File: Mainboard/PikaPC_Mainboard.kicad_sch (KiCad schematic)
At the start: 87 parts, among them J1 Conn_02x08_Odd_Even, J10 Conn_01x08, J11 Conn_01x08, J12 Conn_01x08, J13 Conn_01x08, J14 Conn_01x08, J15 Conn_01x08, J16 Conn_01x08, J17 Conn_01x08, J18 Conn_01x10, J19 Conn_02x05_Odd_Even, J5 DIN41612_03x32_C_Split, J6 Mini-DIN-6, J7 Mini-DIN-6, J9 Conn_01x08, SW1 SW_Push_DPDT, SW2 SW_Push, U1 PPC403GA, U10 74LS07, U11 86C325, U12 GD75232N, U13 74LVC125, U14 MCP120-315GI/TO, U15 AS6C4008-55PCN, U16 AS6C4008-55PCN, U17 ATF1504, U18 T224162B, U19 T224162B, U2 SN74LVC245A, U20 T224162B, U21 T224162B, U22 SN74LVC245A, U23 SN74LVC245A, U3 SST39VF010, U4 SN74LVC245A, U5 SN74LVC245A, U6 SN74LVC245A, U7 8042 PS/2, U8 SN74LVC245A, U9 74LS04, Y1 25M, Y2 7M3728, Y3 14M31818

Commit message: VRAM control debugging
- correct clock edge for VLB ReadyIn
- minor tweaks for S3 ViRGE symbol
- add series resistors to VRAM control signals
- add strapping resistor to support Trio64V+
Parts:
- added RN10, RN11, RN12: 33R, Resistor_THT:R_Array_SIP10, symbol Device:R_Pack05_SIP_Split
- added RN9: 10X-1-472LF, Resistor_THT:R_Array_SIP10, symbol Device:R_Network09_US
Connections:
- net +5V: now also RN9.1 (common)
- net VID-SAUP2: now also RN5.2 (R1)
- net VMA0: now also RN11.1 (R1.1)
- net VMA1: now also RN11.3 (R2.1)
- net VMA2: now also RN11.5 (R3.1)
- net VMA3: now also RN11.7 (R4.1)
- net VMA4: now also RN11.9 (R5.1)
- net VMA5: now also RN12.1 (R1.1)
- net VMA6: now also RN12.3 (R2.1)
- net VMA7: now also RN12.5 (R3.1)
- net VMA8: now also RN12.7 (R4.1)
- net VMD24: now also RN6.7 (R6)
- net ~{VMOE}: now also RN10.5 (R3.1); no longer U18.27 (~{OE}), U19.27 (~{OE}), U20.27 (~{OE}), U21.27 (~{OE})
- net ~{VMRAS0}: now also RN10.1 (R1.1); no longer U18.14 (~{RAS}), U19.14 (~{RAS}), U20.14 (~{RAS}), U21.14 (~{RAS})
- net ~{VMWE}: now also RN10.3 (R2.1); no longer U18.13 (~{WE}), U19.13 (~{WE}), U20.13 (~{WE}), U21.13 (~{WE})
- net VLCLK: now reaches U11.148 (LCLK)
- net VLCLK: now also RN9.2 (R1)
- net VEVIDEO: now reaches U11.203 (~{VREQ})
- net VEVIDEO: now also RN9.5 (R4)
- net ~{VCREQ}: now reaches U11.204 (~{CREQ})
- net ~{VCREQ}: now also RN9.3 (R2)
- net VESYNC: now reaches U11.205 (SPCLK)
- net VESYNC: now also RN9.4 (R3)
- net ~{VBLANK}: now reaches U11.206 (SPD)
- net ~{VBLANK}: now also RN9.6 (R5)
- new net ~{VMOER}: RN10.6 (R3.2), U18.27 (~{OE}), U19.27 (~{OE}), U20.27 (~{OE}), U21.27 (~{OE})
- new net ~{VMRAS0R}: RN10.2 (R1.2), U18.14 (~{RAS}), U19.14 (~{RAS}), U20.14 (~{RAS}), U21.14 (~{RAS})
- new net ~{VMWER}: RN10.4 (R2.2), U18.13 (~{WE}), U19.13 (~{WE}), U20.13 (~{WE}), U21.13 (~{WE})
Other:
- note added: "VMD24 for LPB Mode on Trio64V+"
- moved on the sheet: FB1, FB2, FB3, J1, R11, R6, R7, RN1, RN2, RN3, RN5, U11A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

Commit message: Add new bus to wire-wrap mainboard
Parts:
- removed C19, C20, C21, C22: 47p, Capacitor_THT:C_Disc_D3.0mm_W2.0mm_P2.50mm, symbol Device:C_Small_US
- removed C23, C24: 100nF, Capacitor_THT:C_Disc_D3.0mm_W2.0mm_P2.50mm, symbol Device:C_Small_US
- removed FB1, FB2, FB3: FerriteBead, Inductor_THT:L_Axial_L7.0mm_D3.3mm_P5.08mm_Vertical_Fastron_MICC, symbol Device:FerriteBead
- removed J1: Conn_02x08_Odd_Even, Connector_PinHeader_2.54mm:PinHeader_2x08_P2.54mm_Vertical, symbol Connector_Generic:Conn_02x08_Odd_Even
- removed J6, J7: Mini-DIN-6, Connector_PinHeader_2.54mm:PinHeader_2x03_P2.54mm_Vertical, symbol Connector:Mini-DIN-6
- removed R11, R6, R7: 75R, Resistor_THT:R_Axial_DIN0204_L3.6mm_D1.6mm_P2.54mm_Vertical, symbol Device:R_Small_US
- removed R2: 220R, Resistor_THT:R_Axial_DIN0204_L3.6mm_D1.6mm_P2.54mm_Vertical, symbol Device:R_Small_US
- removed R3: 470R, Resistor_THT:R_Axial_DIN0204_L3.6mm_D1.6mm_P2.54mm_Vertical, symbol Device:R_Small_US
- removed RN10, RN11, RN12: 33R, Resistor_THT:R_Array_SIP10, symbol Device:R_Pack05_SIP_Split
- removed RN4, RN6, RN8: 9A103J, Resistor_THT:R_Array_SIP9, symbol Device:R_Network08_US
- removed RN7: 10X-1-472F, Resistor_THT:R_Array_SIP9, symbol Device:R_Network08_US
- removed RN9: 10X-1-472LF, Resistor_THT:R_Array_SIP10, symbol Device:R_Network09_US
- removed unit 4 of U10
- removed unit 1 of U10
- removed unit 2 of U10
- removed unit 3 of U10
- removed U11: 86C325, Package_QFP:PQFP-208_28x28mm_P0.5mm, symbol PikaPC:S3 86C325 ViRGE
- removed U17: ATF1504, Package_LCC:PLCC-44_THT-Socket, symbol Wrap030-ATX:ATF1504AS
- removed U18, U19, U20, U21: T224162B, Package_SO:SOJ-44_10.16x28.575mm_P1.27mm, symbol PikaPC:T224162B-xJ
- removed U7: 8042 PS/2, Package_DIP:DIP-40_W15.24mm_Socket, symbol MCU_Intel:8040
- removed unit 2 of U9
- removed unit 3 of U9
- removed unit 4 of U9
- removed unit 1 of U9
- removed Y3: 14M31818, Oscillator:Oscillator_DIP-8, symbol Oscillator:CXO_DIP8
- added U102: SN74LVC245A, Package_DIP:DIP-20_W7.62mm_Socket, symbol 74xx:74LS245
- added U109, U110, U111, U112: 74LS244, Package_DIP:DIP-20_W7.62mm_Socket, symbol 74xx:74LS244
- added U2: ATF1508AS, Package_LCC:PLCC-84_THT-Socket, symbol PikaPC:ATF1508AS
- renumbered U8 to U101, U22 to U103, U23 to U104, U2 to U105, U4 to U106, U5 to U107, U6 to U108
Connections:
- net VD0 is gone; now on net D31: U106.2 (A0)
- net VD1 is gone; now on net D30: U106.3 (A1)
- net VD10 is gone; now on net D29: U101.4 (A2), U105.4 (A2)
- net VD11 is gone; now on net D28: U101.5 (A3), U105.5 (A3)
- net VD12 is gone; now on net D27: U101.6 (A4), U105.6 (A4)
- net VD13 is gone; now on net D26: U101.7 (A5), U105.7 (A5)
- net VD14 is gone; now on net D25: U101.8 (A6), U105.8 (A6)
- net VD15 is gone; now on net D24: U101.9 (A7), U105.9 (A7)
- net VD2 is gone; now on net D29: U106.4 (A2)
- net VD3 is gone; now on net D28: U106.5 (A3)
- net VD4 is gone; now on net D27: U106.6 (A4)
- net VD5 is gone; now on net D26: U106.7 (A5)
- net VD6 is gone; now on net D25: U106.8 (A6)
- net VD7 is gone; now on net D24: U106.9 (A7)
- net VD8 is gone; now on net D31: U101.2 (A0), U105.2 (A0)
- net VD9 is gone; now on net D30: U101.3 (A1), U105.3 (A1)
- net ~{PBE2} is gone; now on net ~{BEN-32}: U103.19 (CE)
- net ~{PBE3} is gone; now on net ~{BEN-32}: U104.19 (CE)
- net +12V: now also J5.a30 (Pin_a30)
- net +3.3V: now also J5.a22 (Pin_a22), J5.a23 (Pin_a23), J5.b5 (Pin_b5), J5.b6 (Pin_b6), U102.20 (VCC)
- net +5V: now also J5.a2 (Pin_a2), J5.a31 (Pin_a31), J5.b2 (Pin_b2), J5.b3 (Pin_b3), J5.b31 (Pin_b31), J5.b4 (Pin_b4), J5.c2 (Pin_c2), J5.c31 (Pin_c31), U109.20 (VCC), U110.20 (VCC), U111.20 (VCC), U112.20 (VCC), U2.13 (VCCIO), U2.26 (VCCIO), U2.3 (VCC), U2.38 (VCCIO), U2.43 (VCC), U2.53 (VCCIO), U2.66 (VCCIO), U2.78 (VCCIO)
- net -12V: now also J5.c30 (Pin_c30)
- net A0/~{WBE0}: now also U2.41 (IO49)
- net A10: now also U110.6 (I2a)
- net A11: now also U110.8 (I3a)
- net A12: now also U110.11 (I0b)
- net A13: now also U110.13 (I1b)
- net A14: now also U110.15 (I2b)
- net A15: now also U110.17 (I3b)
- net A16: now also U111.2 (I0a)
- net A17: now also U111.4 (I1a)
- net A18: now also U111.6 (I2a)
- net A19: now also U111.8 (I3a)
- net A1/~{WBE1}: now also U2.40 (IO51)
- net A2: now also U109.6 (I2a)
- net A20: now also U111.11 (I0b)
- net A21: now also U111.13 (I1b)
- net A22: now also U111.15 (I2b)
- net A23: now also U111.17 (I3b)
- net A24: now also U112.2 (I0a)
- net A25: now also U112.4 (I1a)
- net A3: now also U109.8 (I3a)
- net A4: now also U109.11 (I0b)
- net A5: now also U109.13 (I1b)
- net A6: now also U109.15 (I2b)
- net A7: now also U109.17 (I3b)
- net A8: now also U110.2 (I0a)
- net A9: now also U110.4 (I1a)
- net D0: now also U104.9 (A7); no longer U107.18 (B0)
- net D1: now also U104.8 (A6); no longer U107.17 (B1)
- net D10: now also U103.7 (A5); no longer U108.16 (B2)
- net D11: now also U103.6 (A4); no longer U108.15 (B3)
- net D12: now also U103.5 (A3); no longer U108.14 (B4)
- net D13: now also U103.4 (A2); no longer U108.13 (B5)
- net D14: now also U103.3 (A1); no longer U108.12 (B6)
- net D15: now also U103.2 (A0); no longer U108.11 (B7)
- net D16: now also U108.9 (A7), U102.9 (A7); no longer U105.18 (B0)
- net D17: now also U108.8 (A6), U102.8 (A6); no longer U105.17 (B1)
- net D18: now also U108.7 (A5), U102.7 (A5); no longer U105.16 (B2)
- net D19: now also U108.6 (A4), U102.6 (A4); no longer U105.15 (B3)
- net D2: now also U104.7 (A5); no longer U107.16 (B2)
- net D20: now also U108.5 (A3), U102.5 (A3); no longer U105.14 (B4)
- net D21: now also U108.4 (A2), U102.4 (A2); no longer U105.13 (B5)
- net D22: now also U108.3 (A1), U102.3 (A1); no longer U105.12 (B6)
- net D23: now also U108.2 (A0), U102.2 (A0); no longer U105.11 (B7)
- net D24: now also U107.9 (A7); no longer U101.18 (B0), U103.18 (B0), U104.18 (B0), U106.18 (B0)
- net D25: now also U107.8 (A6); no longer U101.17 (B1), U103.17 (B1), U104.17 (B1), U106.17 (B1)
- net D26: now also U107.7 (A5); no longer U101.16 (B2), U103.16 (B2), U104.16 (B2), U106.16 (B2)
- net D27: now also U107.6 (A4); no longer U101.15 (B3), U103.15 (B3), U104.15 (B3), U106.15 (B3)
- net D28: now also U107.5 (A3); no longer U101.14 (B4), U103.14 (B4), U104.14 (B4), U106.14 (B4)
- net D29: now also U107.4 (A2); no longer U101.13 (B5), U103.13 (B5), U104.13 (B5), U106.13 (B5)
- net D3: now also U104.6 (A4); no longer U107.15 (B3)
- net D30: now also U107.3 (A1); no longer U101.12 (B6), U103.12 (B6), U104.12 (B6), U106.12 (B6)
- net D31: now also U107.2 (A0); no longer U101.11 (B7), U103.11 (B7), U104.11 (B7), U106.11 (B7)
- net D4: now also U104.5 (A3); no longer U107.14 (B4)
- net D5: now also U104.4 (A2); no longer U107.13 (B5)
- net D6: now also U104.3 (A1); no longer U107.12 (B6)
- net D7: now also U104.2 (A0); no longer U107.11 (B7)
- net D8: now also U103.9 (A7); no longer U108.18 (B0)
- net D9: now also U103.8 (A6); no longer U108.17 (B1)
- net GND: now also J5.a1 (Pin_a1), J5.a28 (Pin_a28), J5.a32 (Pin_a32), J5.b1 (Pin_b1), J5.b10 (Pin_b10), J5.b11 (Pin_b11), J5.b12 (Pin_b12), J5.b13 (Pin_b13), J5.b14 (Pin_b14), J5.b15 (Pin_b15), J5.b16 (Pin_b16), J5.b17 (Pin_b17), J5.b18 (Pin_b18), J5.b19 (Pin_b19), J5.b20 (Pin_b20), J5.b21 (Pin_b21), J5.b28 (Pin_b28), J5.b29 (Pin_b29), J5.b30 (Pin_b30), J5.b32 (Pin_b32), J5.b7 (Pin_b7), J5.b8 (Pin_b8), J5.b9 (Pin_b9), J5.c1 (Pin_c1), J5.c29 (Pin_c29), J5.c32 (Pin_c32), U102.10 (GND), U109.10 (GND), U109.2 (I0a), U109.4 (I1a), U110.10 (GND), U111.10 (GND), U112.10 (GND), U112.17 (I3b), U112.6 (I2a), U112.8 (I3a), U2.19 (GND), U2.32 (GND), U2.42 (GND), U2.47 (GND), U2.59 (GND), U2.7 (GND), U2.72 (GND), U2.82 (GND)
- net HoldAck: now also U2.49 (IO73)
- net HoldReq: now also U2.48 (IO72)
- net INT0: now also U2.67 (IO104)
- net INT1: now also U2.68 (IO105)
- net INT2: now also U2.69 (IO107)
- net INT3: now also U2.70 (IO109)
- net INT4: now also U2.73 (IO115)
- net Ready: now also U2.50 (IO75)
- net R/~{W}: now also U2.12 (IO3); no longer U101.1 (A->B), U103.1 (A->B), U104.1 (A->B), U105.1 (A->B), U106.1 (A->B), U107.1 (A->B), U108.1 (A->B)
- net SysClk-5v: now also U2.83 (GCLK1)
- net ~{CINT}: now also U2.44 (IO65)
- net ~{CS0}: now also U2.54 (IO83)
- net ~{CS1}: now also U2.55 (IO85)
- net ~{CS2}: now also U2.56 (IO86)
- net ~{CS3}: now also U2.57 (IO88)
- net ~{CS4}: now also U2.58 (IO91)
- net ~{CS5}: now also U2.60 (IO93)
- net ~{CS6}: now also U2.61 (IO94)
- net ~{CS7}: now also U2.63 (IO97)
- net ~{Reset}: now also U2.1 (GCLR)
- net ~{WBE2}: now also U2.39 (IO53)
- net ~{WBE3}: now also U2.37 (IO56)
- net AD8: now reaches J5.c10 (Pin_c10)
- net AD8: now also U103.11 (B7), U106.11 (B7), U110.18 (O0a)
- net AD10: now reaches J5.c11 (Pin_c11)
- net AD10: now also U103.13 (B5), U106.13 (B5), U110.14 (O2a)
- net AD12: now reaches J5.c12 (Pin_c12)
- net AD12: now also U103.15 (B3), U106.15 (B3), U110.9 (O0b)
- net AD14: now reaches J5.c13 (Pin_c13)
- net AD14: now also U103.17 (B1), U106.17 (B1), U110.5 (O2b)
- net AD16: now reaches J5.c14 (Pin_c14)
- net AD16: now also U105.11 (B7), U102.11 (B7), U111.18 (O0a)
- net AD18: now reaches J5.c15 (Pin_c15)
- net AD18: now also U105.13 (B5), U102.13 (B5), U111.14 (O2a)
- net AD20: now reaches J5.c16 (Pin_c16)
- net AD20: now also U105.15 (B3), U102.15 (B3), U111.9 (O0b)
- net AD22: now reaches J5.c17 (Pin_c17)
- net AD22: now also U105.17 (B1), U102.17 (B1), U111.5 (O2b)
- net AD24: now reaches J5.c18 (Pin_c18)
- net AD24: now also U101.11 (B7), U112.18 (O0a)
- net AD26: now reaches J5.c19 (Pin_c19)
- net AD26: now also U101.13 (B5), U112.14 (O2a)
- net AD28: now reaches J5.c20 (Pin_c20)
- net AD28: now also U101.15 (B3), U112.9 (O0b)
- net AD30: now reaches J5.c21 (Pin_c21)
- net AD30: now also U101.17 (B1), U112.5 (O2b)
- net ~{Bus-REQ}: now reaches J5.c22 (Pin_c22)
- net ~{Bus-REQ}: now also U2.77 (IO123)
- net ~{Bus-GNT}: now reaches J5.c23 (Pin_c23)
- net ~{Bus-GNT}: now also U2.81 (IO128)
- net ~{Bus-BE0}: now reaches J5.c24 (Pin_c24)
- net ~{Bus-BE0}: now also U2.21 (IO19)
- net ~{Bus-BE2}: now reaches J5.c25 (Pin_c25)
- net ~{Bus-BE2}: now also U2.16 (IO27)
- net ~{Bus-BRACK}: now reaches J5.c26 (Pin_c26)
- net ~{Bus-Start}: now reaches J5.c27 (Pin_c27)
- net ~{Bus-Start}: now also U2.15 (IO29)
- net ~{Bus-BERR}: now reaches J5.c28 (Pin_c28)
- net ~{Bus-Reset}: now reaches J5.c3 (Pin_c3)
- net ~{Bus-IACK}: now reaches J5.c4 (Pin_c4)
- net Bus-R/~{W}: now reaches J5.c5 (Pin_c5)
- net AD0: now reaches J5.c6 (Pin_c6)
- net AD0: now also U104.11 (B7), U107.11 (B7), U108.11 (B7), U109.18 (O0a)
- net AD2: now reaches J5.c7 (Pin_c7)
- net AD2: now also U104.13 (B5), U107.13 (B5), U108.13 (B5), U109.14 (O2a)
- net AD4: now reaches J5.c8 (Pin_c8)
- net AD4: now also U104.15 (B3), U107.15 (B3), U108.15 (B3), U109.9 (O0b)
- net AD6: now reaches J5.c9 (Pin_c9)
- net AD6: now also U104.17 (B1), U107.17 (B1), U108.17 (B1), U109.5 (O2b)
- net AD9: now reaches J5.a10 (Pin_a10)
- net AD9: now also U103.12 (B6), U106.12 (B6), U110.16 (O1a)
- net AD11: now reaches J5.a11 (Pin_a11)
- net AD11: now also U103.14 (B4), U106.14 (B4), U110.12 (O3a)
- net AD13: now reaches J5.a12 (Pin_a12)
- net AD13: now also U103.16 (B2), U106.16 (B2), U110.7 (O1b)
- net AD15: now reaches J5.a13 (Pin_a13)
- net AD15: now also U103.18 (B0), U106.18 (B0), U110.3 (O3b)
- net AD17: now reaches J5.a14 (Pin_a14)
- net AD17: now also U105.12 (B6), U102.12 (B6), U111.16 (O1a)
- net AD19: now reaches J5.a15 (Pin_a15)
- net AD19: now also U105.14 (B4), U102.14 (B4), U111.12 (O3a)
- net AD21: now reaches J5.a16 (Pin_a16)
- net AD21: now also U105.16 (B2), U102.16 (B2), U111.7 (O1b)
- net AD23: now reaches J5.a17 (Pin_a17)
- net AD23: now also U105.18 (B0), U102.18 (B0), U111.3 (O3b)
- net AD25: now reaches J5.a18 (Pin_a18)
- net AD25: now also U101.12 (B6), U112.16 (O1a)
- net AD27: now reaches J5.a19 (Pin_a19)
- net AD27: now also U101.14 (B4), U112.12 (O3a)
- net AD29: now reaches J5.a20 (Pin_a20)
- net AD29: now also U101.16 (B2), U112.7 (O1b)
- net AD31: now reaches J5.a21 (Pin_a21)
- net AD31: now also U101.18 (B0), U112.3 (O3b)
- net ~{Bus-BE1}: now reaches J5.a24 (Pin_a24)
- net ~{Bus-BE1}: now also U2.18 (IO24)
- net ~{Bus-BE3}: now reaches J5.a25 (Pin_a25)
- net ~{Bus-BE3}: now also U2.17 (IO25)
- net ~{Bus-BURST}: now reaches J5.a26 (Pin_a26)
- net ~{Bus-ACK}: now reaches J5.a27 (Pin_a27)
- net ~{Bus-ACK}: now also U2.20 (IO21)
- net Bus-Clk: now reaches J5.a29 (Pin_a29)
- net ~{Bus-IRQ0}: now reaches J5.a3 (Pin_a3)
- net ~{Bus-IRQ0}: now also U2.6 (IO13)
- net ~{Bus-IRQ1}: now reaches J5.a4 (Pin_a4)
- net ~{Bus-IRQ1}: now also U2.5 (IO14)
- net ~{Bus-IRQ2}: now reaches J5.a5 (Pin_a5)
- net ~{Bus-IRQ2}: now also U2.4 (IO16)
- net AD1: now reaches J5.a6 (Pin_a6)
- net AD1: now also U104.12 (B6), U107.12 (B6), U108.12 (B6), U109.16 (O1a)
- net AD3: now reaches J5.a7 (Pin_a7)
- net AD3: now also U104.14 (B4), U107.14 (B4), U108.14 (B4), U109.12 (O3a)
- net AD5: now reaches J5.a8 (Pin_a8)
- net AD5: now also U104.16 (B2), U107.16 (B2), U108.16 (B2), U109.7 (O1b)
- net AD7: now reaches J5.a9 (Pin_a9)
- net AD7: now also U104.18 (B0), U107.18 (B0), U108.18 (B0), U109.3 (O3b)
- removed net VD16: U103.2 (A0), U108.2 (A0)
- removed net VD17: U103.3 (A1), U108.3 (A1)
- removed net VD18: U103.4 (A2), U108.4 (A2)
- removed net VD19: U103.5 (A3), U108.5 (A3)
- removed net VD20: U103.6 (A4), U108.6 (A4)
- removed net VD21: U103.7 (A5), U108.7 (A5)
- removed net VD22: U103.8 (A6), U108.8 (A6)
- removed net VD23: U103.9 (A7), U108.9 (A7)
- removed net VD24: U104.2 (A0), U107.2 (A0)
- removed net VD25: U104.3 (A1), U107.3 (A1)
- removed net VD26: U104.4 (A2), U107.4 (A2)
- removed net VD27: U104.5 (A3), U107.5 (A3)
- removed net VD28: U104.6 (A4), U107.6 (A4)
- removed net VD29: U104.7 (A5), U107.7 (A5)
- removed net VD30: U104.8 (A6), U107.8 (A6)
- removed net VD31: U104.9 (A7), U107.9 (A7)
- removed net ~{PB32}: U105.19 (CE), U107.19 (CE), U108.19 (CE)
- net ~{PBE0} renamed ~{BEN-8-1}
- net ~{BEN-8-1}: now also U2.25 (IO45)
- net ~{PBE1} renamed ~{BEN-32}
- net ~{BEN-32}: now also U102.19 (CE), U2.31 (IO35)
- new net BDDIR: U101.1 (A->B), U102.1 (A->B), U103.1 (A->B), U104.1 (A->B), U105.1 (A->B), U106.1 (A->B), U107.1 (A->B), U108.1 (A->B), U2.24 (IO46)
- new net XA1: U112.15 (I2b), U2.30 (IO37)
- new net XA2: U112.13 (I1b), U2.29 (IO38)
- new net XA3: U112.11 (I0b), U2.28 (IO40)
- new net ~{AEN}: U109.1 (OEa), U109.19 (OEb), U110.1 (OEa), U110.19 (OEb), U111.1 (OEa), U111.19 (OEb), U112.1 (OEa), U112.19 (OEb), U2.27 (IO43)
- new net ~{BEN-16}: U108.19 (CE), U2.34 (IO61)
- new net ~{BEN-8-0}: U107.19 (CE), U2.36 (IO57)
- new net ~{BEN-8-2}: U105.19 (CE), U2.22 (IO17)
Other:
- note added: "Expansion Bus Buffers"
- note added: "Expansion Bus Control"
- note added: "LSB"
- note added: "MSB"
- note removed: "PS/2 Keyboard/Mouse"
- note removed: "Peripheral Bus Control"
- note removed: "RN8 for slow VRAM cycles"
- note removed: "RSET Target: 147R"
- note removed: "VMD24 for LPB Mode on Trio64V+"
- note removed: "Video"
- moved on the sheet: J5A, J5B, J5C, U101, U103, U104, U105, U106, U107, U108, U13A

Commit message: new bus control logic
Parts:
- added R2: 4k7, Resistor_THT:R_Axial_DIN0204_L3.6mm_D1.6mm_P7.62mm_Horizontal, symbol Device:R_Small_US
- added RN4: 10X-1-102LF, Resistor_THT:R_Array_SIP10, symbol Device:R_Network09_US
- added U4: 74AHCT244, Package_DIP:DIP-20_W7.62mm_Socket, symbol 74xx:74LS244
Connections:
- net +5V: now also R2.1, RN4.1 (common), U4.20 (VCC)
- net Bus-Clk: now also U4.18 (O0a)
- net Bus-R/~{W}: now also U4.12 (O3a)
- net GND: now also U4.1 (OEa), U4.10 (GND)
- net INT0: now also RN3.3 (R2)
- net INT1: now also RN3.4 (R3)
- net INT2: now also RN3.5 (R4)
- net Ready: no longer U13.3
- net R/~{W}: now also U4.8 (I3a)
- net SysClk-5v: now also U4.2 (I0a)
- net ~{Bus-ACK}: now also RN4.6 (R5)
- net ~{Bus-BERR}: now also RN4.8 (R7)
- net ~{Bus-BRACK}: now also RN4.7 (R6)
- net ~{Bus-IRQ0}: now also RN4.2 (R1)
- net ~{Bus-IRQ1}: now also RN4.3 (R2)
- net ~{Bus-IRQ2}: now also RN4.4 (R3)
- net ~{Bus-REQ}: now also RN4.5 (R4)
- net ~{VID-SRDY}: no longer names the net of U13.1
- new net: R2.2, U4.19 (OEb)
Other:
- moved on the sheet: U13A

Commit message: SIMM72 card logic
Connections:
- net +5V: no longer R2.1
- net GND: now also R2.1
- net ~{Bus-Reset}: now also U4.3 (O3b)
- net ~{Reset}: now also U4.17 (I3b)
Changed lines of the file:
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@@
 	(wire
 		(pts
+			(xy 571.5 165.1) (xy 584.2 165.1)
+		)
+		(stroke
+			(width 0)
+			(type default)
+		)
+	)
+	(wire
+		(pts
 			(xy 381 116.84) (xy 393.7 116.84)
 		)
@@
 	(wire
 		(pts
+			(xy 622.3 165.1) (xy 609.6 165.1)
+		)
+		(stroke
+			(width 0)
+			(type default)
+		)
+	)
+	(wire
+		(pts
 			(xy 48.26 251.46) (xy 48.26 248.92)
 		)
@@
 		)
 	)
+	(label "~{Reset}"
+		(at 571.5 165.1 0)
+		(effects
+			(font
+				(size 1.27 1.27)
+			)
+			(justify left bottom)
+		)
+	)
 	(label "VID-SAUP2"
 		(at 228.6 154.94 0)
@@
 		)
 	)
+	(label "~{Bus-Reset}"
+		(at 622.3 165.1 180)
+		(effects
+			(font
+				(size 1.27 1.27)
+			)
+			(justify right bottom)
+		)
+	)
 	(label "~{Bus-IRQ1}"
 		(at 441.96 55.88 0)
@@
 	)
 	(symbol
+		(lib_id "power:GND")
+		(at 566.42 172.72 270)
+		(unit 1)
+		(exclude_from_sim no)
+		(in_bom yes)
+		(on_board yes)
+		(dnp no)
+		(fields_autoplaced yes)
+		(property "Reference" "#PWR0152"
+			(at 560.07 172.72 0)
+			(effects
+				(font
+					(size 1.27 1.27)
+				)
+				(hide yes)
+			)
+		)
+		(property "Value" "GND"
+			(at 563.2451 172.72 90)
+			(effects
+				(font
+					(size 1.27 1.27)
+				)
+				(justify right)
+			)
+		)
+		(property "Footprint" ""
+			(at 566.42 172.72 0)
+			(effects
+				(font
+					(size 1.27 1.27)
+				)
+				(hide yes)
+			)
+		)
+		(property "Datasheet" ""
+			(at 566.42 172.72 0)
+			(effects
+				(font
+					(size 1.27 1.27)
+				)
+				(hide yes)
+			)
+		)
+		(property "Description" "Power symbol creates a global label with name \"GND\" , ground"
+			(at 566.42 172.72 0)
+			(effects
+				(font
+					(size 1.27 1.27)
+				)
+				(hide yes)
+			)
+		)
+		(pin "1"
+		)
+		(instances
+			(project "PikaPC_Mainboard"
+				(path "/31647a00-1631-4687-a4ca-8a073377aae5"
+					(reference "#PWR0152")
+					(unit 1)
+				)
+			)
+		)
+	)
+	(symbol
 		(lib_id "power:+5V")
 		(at 474.98 50.8 90)
@@
 				)
 			)
-		)
-	)
-	(symbol
-		(lib_id "power:+5V")
-		(at 566.42 172.72 90)
-		(unit 1)
-		(exclude_from_sim no)
-		(in_bom yes)
-		(on_board yes)
-		(dnp no)
-		(fields_autoplaced yes)
-		(property "Reference" "#PWR0152"
-			(at 570.23 172.72 0)
-			(effects
-				(font
-					(size 1.27 1.27)
-				)
-				(hide yes)
-			)
-		)
-		(property "Value" "+5V"
-			(at 563.2451 172.72 90)
-			(effects
-				(font
-					(size 1.27 1.27)
-				)
-				(justify left)
-			)
-		)
-		(property "Footprint" ""
-			(at 566.42 172.72 0)
-			(effects
-				(font
-					(size 1.27 1.27)
-				)
-				(hide yes)
-			)
-		)
-		(property "Datasheet" ""
-			(at 566.42 172.72 0)
-			(effects
-				(font
-					(size 1.27 1.27)
-				)
-				(hide yes)
-			)
-		)
-		(property "Description" "Power symbol creates a global label with name \"+5V\""
-			(at 566.42 172.72 0)
-			(effects
-				(font
-					(size 1.27 1.27)
-				)
-				(hide yes)
-			)
-		)
-		(pin "1"
-		)
-		(instances
-			(project "PikaPC_Mainboard"
-				(path "/31647a00-1631-4687-a4ca-8a073377aae5"
-					(reference "#PWR0152")
-					(unit 1)
-				)
-			)

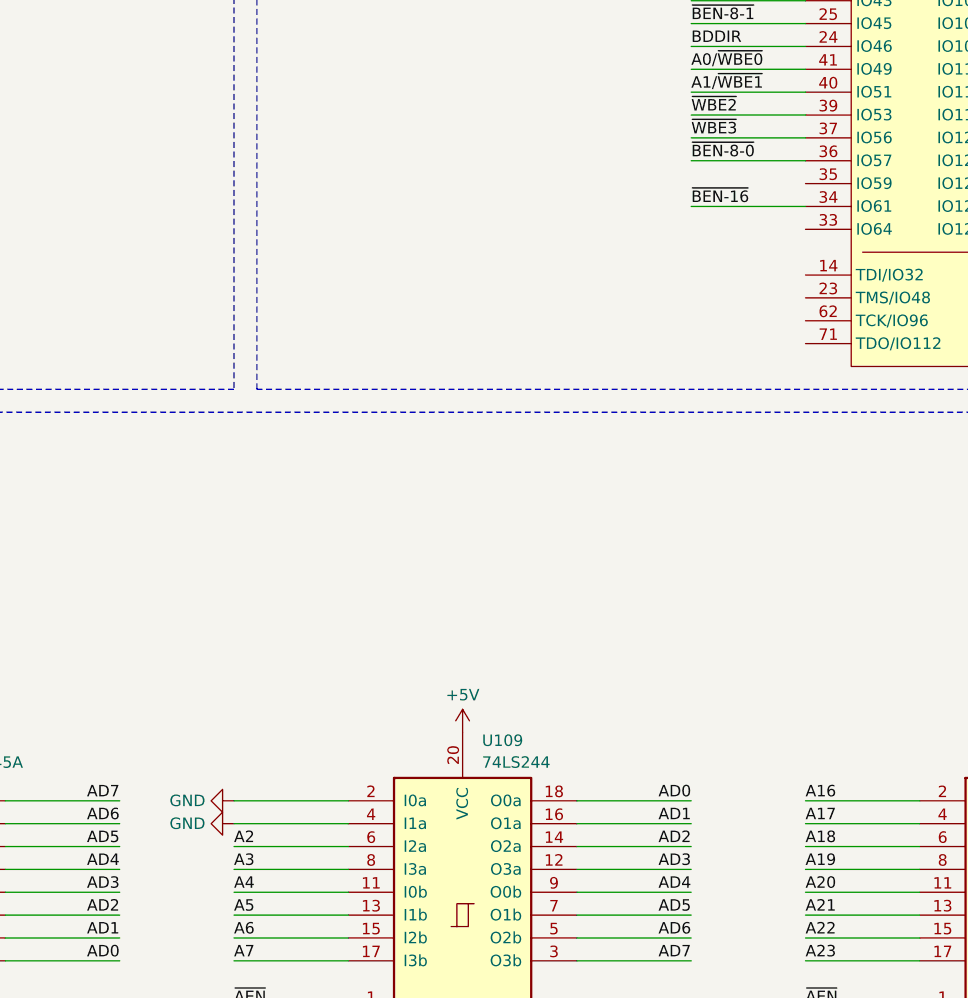
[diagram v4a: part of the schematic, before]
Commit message: fix low two expansion bus address bits
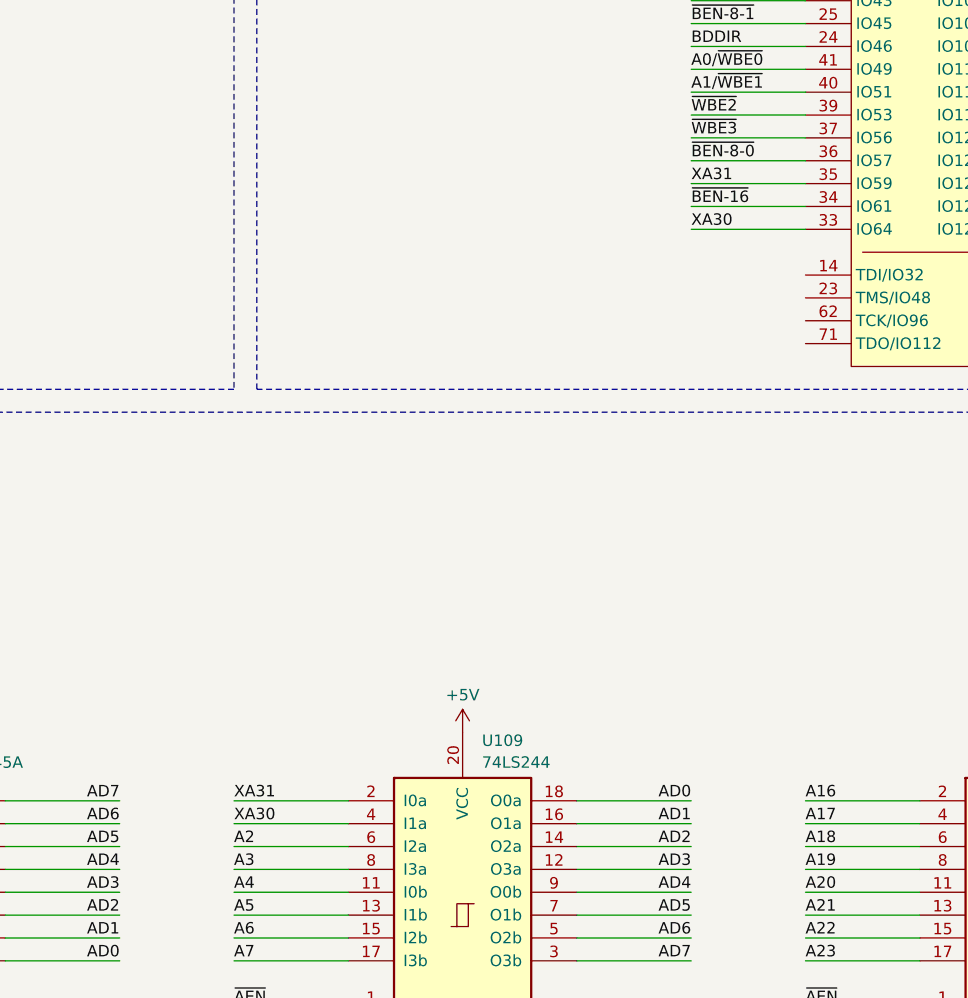
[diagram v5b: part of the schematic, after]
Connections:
- net GND: no longer U109.2 (I0a), U109.4 (I1a)
- net XA30: now reaches U2.33 (IO64)
- net XA30: now also U109.4 (I1a)
- net XA31: now reaches U2.35 (IO59)
- net XA31: now also U109.2 (I0a)
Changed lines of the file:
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@@
 	(wire
 		(pts
+			(xy 469.9 261.62) (xy 457.2 261.62)
+		)
+		(stroke
+			(width 0)
+			(type default)
+		)
+	)
+	(wire
+		(pts
 			(xy 160.02 116.84) (xy 160.02 114.3)
 		)
@@
 	(wire
 		(pts
+			(xy 469.9 256.54) (xy 457.2 256.54)
+		)
+		(stroke
+			(width 0)
+			(type default)
+		)
+	)
+	(wire
+		(pts
 			(xy 73.66 215.9) (xy 73.66 218.44)
 		)
@@
 		)
 	)
+	(label "XA31"
+		(at 457.2 256.54 0)
+		(effects
+			(font
+				(size 1.27 1.27)
+			)
+			(justify left bottom)
+		)
+	)
 	(label "D28"
 		(at 342.9 332.74 0)
@@
 		)
 	)
+	(label "XA30"
+		(at 406.4 327.66 0)
+		(effects
+			(font
+				(size 1.27 1.27)
+			)
+			(justify left bottom)
+		)
+	)
 	(label "A2"
 		(at 342.9 104.14 0)
@@
 		)
 	)
+	(label "XA31"
+		(at 406.4 325.12 0)
+		(effects
+			(font
+				(size 1.27 1.27)
+			)
+			(justify left bottom)
+		)
+	)
 	(label "~{CS4}"
 		(at 142.24 119.38 180)
@@
 		)
 	)
+	(label "XA30"
+		(at 457.2 261.62 0)
+		(effects
+			(font
+				(size 1.27 1.27)
+			)
+			(justify left bottom)
+		)
+	)
 	(label "~{CINT}"
 		(at 508 187.96 180)
@@
 	)
 	(symbol
-		(lib_id "power:GND")
-		(at 406.4 325.12 270)
-		(unit 1)
-		(exclude_from_sim no)
-		(in_bom yes)
-		(on_board yes)
-		(dnp no)
-		(fields_autoplaced yes)
-		(property "Reference" "#PWR062"
-			(at 400.05 325.12 0)
-			(effects
-				(font
-					(size 1.27 1.27)
-				)
-				(hide yes)
-			)
-		)
-		(property "Value" "GND"
-			(at 403.2251 325.12 90)
-			(effects
-				(font
-					(size 1.27 1.27)
-				)
-				(justify right)
-			)
-		)
-		(property "Footprint" ""
-			(at 406.4 325.12 0)
-			(effects
-				(font
-					(size 1.27 1.27)
-				)
-				(hide yes)
-			)
-		)
-		(property "Datasheet" ""
-			(at 406.4 325.12 0)
-			(effects
-				(font
-					(size 1.27 1.27)
-				)
-				(hide yes)
-			)
-		)
-		(property "Description" "Power symbol creates a global label with name \"GND\" , ground"
-			(at 406.4 325.12 0)
-			(effects
-				(font
-					(size 1.27 1.27)
-				)
-				(hide yes)
-			)
-		)
-		(pin "1"
-		)
-		(instances
-			(project "PikaPC_Mainboard"
-				(path "/31647a00-1631-4687-a4ca-8a073377aae5"
-					(reference "#PWR062")
-					(unit 1)
-				)
-			)
-		)
-	)
-	(symbol
 		(lib_id "power:+3.3V")
 		(at 441.96 101.6 90)
@@
 					(unit 1)
 				)
-			)
-		)
-	)
-	(symbol
-		(lib_id "power:GND")
-		(at 406.4 327.66 270)
-		(unit 1)
-		(exclude_from_sim no)
-		(in_bom yes)
-		(on_board yes)
-		(dnp no)
-		(fields_autoplaced yes)
-		(property "Reference" "#PWR063"
-			(at 400.05 327.66 0)
-			(effects
-				(font
-					(size 1.27 1.27)
-				)
-				(hide yes)
-			)
-		)
-		(property "Value" "GND"
-			(at 403.2251 327.66 90)
-			(effects
-				(font
-					(size 1.27 1.27)
-				)
-				(justify right)
-			)
-		)
-		(property "Footprint" ""
-			(at 406.4 327.66 0)
-			(effects
-				(font
-					(size 1.27 1.27)
-				)
-				(hide yes)
-			)
-		)
-		(property "Datasheet" ""
-			(at 406.4 327.66 0)
-			(effects
-				(font
-					(size 1.27 1.27)
-				)
-				(hide yes)
-			)
-		)
-		(property "Description" "Power symbol creates a global label with name \"GND\" , ground"
-			(at 406.4 327.66 0)
-			(effects
-				(font
-					(size 1.27 1.27)
-				)
-				(hide yes)
-			)
-		)
-		(pin "1"
-		)
-		(instances
-			(project "PikaPC_Mainboard"
-				(path "/31647a00-1631-4687-a4ca-8a073377aae5"
-					(reference "#PWR063")
-					(unit 1)
-				)
